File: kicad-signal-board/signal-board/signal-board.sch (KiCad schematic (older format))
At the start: 24 parts, among them IC1 74HCT245, U1 ESP32-DEVKITC-32D

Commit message: BOM made
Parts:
- removed I2C, TX/RX, sig1, sig2, sig3, sig4, sig5, sig6, sig7, sig8: signal, symbol Connector:Conn_01x02_Male
- added C3, C4: 0.1µF, symbol Device:CP1_Small
- added J1: Conn_02x09_Odd_Even, symbol Connector_Generic:Conn_02x09_Odd_Even
- added J?: Conn_02x08_Odd_Even, symbol Connector_Generic:Conn_02x08_Odd_Even
- added R10, R12: 1k, symbol Device:R_Small_US
- added R11, R13: 10k, symbol Device:R_Small_US
- added SW1, SW2: SW_MEC_5G, symbol Switch:SW_MEC_5G
- gave numbers to parts that had none: 3
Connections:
- wire segments 89 -> 135
- no-connect marks 5 -> 9
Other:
- note removed: "cap and resistor for led\n cap - .1 microferads, 100 nanoferads, 0804 / 1206\n resistor - 150 ohm\nconnect some io pins to jumpers\ntwo buttons - hardware debounce\n\n\n\n"

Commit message: some footprints
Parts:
- R1: renamed from R10; footprint (none) -> Resistor_SMD:R_0805_2012Metric_Pad1.15x1.40mm_HandSolder
- R10: renamed from R5; footprint (none) -> Resistor_SMD:R_0805_2012Metric_Pad1.15x1.40mm_HandSolder
- R11: renamed from R6; footprint (none) -> Resistor_SMD:R_0805_2012Metric_Pad1.15x1.40mm_HandSolder
- R12: renamed from R7; footprint (none) -> Resistor_SMD:R_0805_2012Metric_Pad1.15x1.40mm_HandSolder
- R13: renamed from R8; footprint (none) -> Resistor_SMD:R_0805_2012Metric_Pad1.15x1.40mm_HandSolder
- R2: renamed from R11; footprint (none) -> Resistor_SMD:R_0805_2012Metric_Pad1.15x1.40mm_HandSolder
- R3: renamed from R12; footprint (none) -> Resistor_SMD:R_0805_2012Metric_Pad1.15x1.40mm_HandSolder
- R4: renamed from R9; footprint (none) -> Resistor_SMD:R_0805_2012Metric_Pad1.15x1.40mm_HandSolder
- R5: renamed from R13; footprint (none) -> Resistor_SMD:R_0805_2012Metric_Pad1.15x1.40mm_HandSolder
- R6: renamed from R1; footprint (none) -> Resistor_SMD:R_0805_2012Metric_Pad1.15x1.40mm_HandSolder
- R7: renamed from R2; footprint (none) -> Resistor_SMD:R_0805_2012Metric_Pad1.15x1.40mm_HandSolder
- R8: renamed from R3; footprint (none) -> Resistor_SMD:R_0805_2012Metric_Pad1.15x1.40mm_HandSolder
- R9: renamed from R4; footprint (none) -> Resistor_SMD:R_0805_2012Metric_Pad1.15x1.40mm_HandSolder
- gave numbers to parts that had none: 1
- renumbered C3 to C1, C4 to C2, C2 to C3, C1 to C4, SW2 to SW1, SW1 to SW2
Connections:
- net labels added: +5V
- net labels removed: 5v, GNDREF
- wire segments 135 -> 138
- no-connect marks 9 -> 13
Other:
- moved on the sheet: C1, C2, C3, C4, D1, J1, J2, R1, R10, R11, R12, R13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

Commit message: Copied power supply circuit into signal board schematic, initial creation of PCB
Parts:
- added C5: 100uF, Capacitor_THT:CP_Radial_D5.0mm_P2.50mm, symbol Device:CP1_Small
- added C6: 470pF, Capacitor_SMD:C_1206_3216Metric_Pad1.42x1.75mm_HandSolder, symbol Device:CP1_Small
- added C7: 220uF, Capacitor_SMD:CP_Elec_10x10, symbol Device:CP1_Small
- added D2: 1N5819, Diode_SMD:D_SOD-123, symbol Device:D_Schottky
- added J3: 5V Pwr Conn, Connector_PinHeader_1.00mm:PinHeader_1x02_P1.00mm_Vertical, symbol Connector:Conn_01x02_Male
- added J4: 24V Screw Term, TerminalBlock_TE-Connectivity:TerminalBlock_TE_282834-2_1x02_P2.54mm_Horizontal, symbol Connector:Screw_Terminal_01x02
- added L1: 220uH, Inductor_SMD:L_Bourns-SRR1005, symbol Device:L
- added R14: 0.33 ohms, Resistor_SMD:R_0805_2012Metric_Pad1.15x1.40mm_HandSolder, symbol Device:R_Small_US
- added R15: 1.2K, Resistor_SMD:R_0805_2012Metric_Pad1.15x1.40mm_HandSolder, symbol Device:R_Small_US
- added R16: 3.8K, Resistor_SMD:R_0805_2012Metric_Pad1.15x1.40mm_HandSolder, symbol Device:R_Small_US
- added U2: MC33063AD, Package_SO:SOIC-8_3.9x4.9mm_P1.27mm, symbol Regulator_Switching:MC33063AD
- IC1: symbol 74HCT245:74HCT245 -> signal-board-rescue:74HCT245-74HCT245
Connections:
- net labels added: +24V, 5V_Out, 7V_to_24V_Input, Switching_Power_Supply
- wire segments 138 -> 178
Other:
- moved on the sheet: C1, C2, C3, C4, D1, J1, J2, R1, R10, R11, R12, R13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

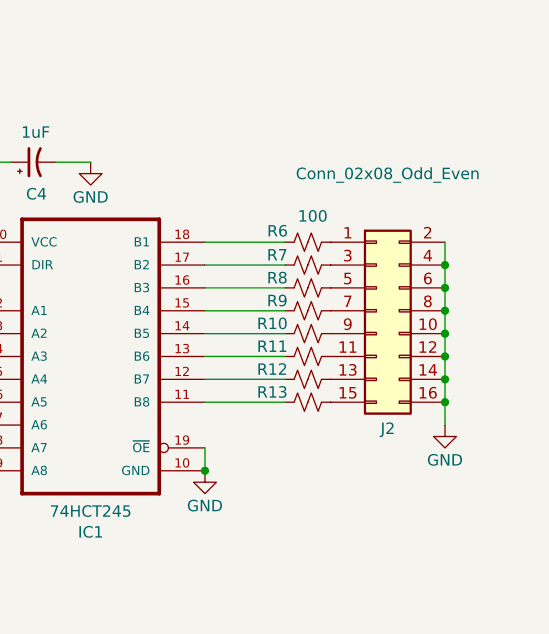
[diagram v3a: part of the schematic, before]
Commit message: More footprints and rough layout of pcb
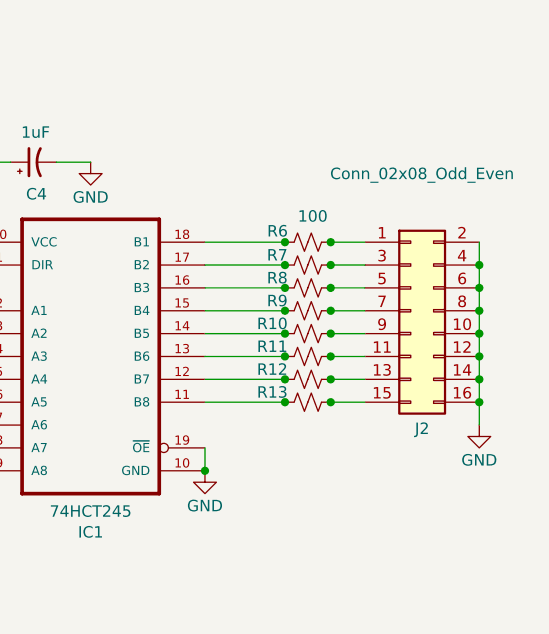
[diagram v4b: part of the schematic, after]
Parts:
- C1, C3: footprint (none) -> Capacitor_SMD:C_0805_2012Metric_Pad1.15x1.40mm_HandSolder
- C2: footprint (none) -> Capacitor_SMD:C_0805_2012Metric_Pad1.15x1.40mm_HandSolder; Supplier Part 08055C104KAT2A -> 478-1395-1-ND
- C4: footprint (none) -> Capacitor_SMD:C_0805_2012Metric_Pad1.15x1.40mm_HandSolder; Supplier Part CC0805KKX7R7BB105 -> 311-1365-1-ND
- IC1: footprint (none) -> Package_SO:SOIC-20W_7.5x12.8mm_P1.27mm
- J1: footprint (none) -> Connector_PinHeader_2.54mm:PinHeader_2x09_P2.54mm_Vertical
- J2: footprint (none) -> Connector_PinHeader_2.54mm:PinHeader_2x08_P2.54mm_Vertical
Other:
- moved on the sheet: J2
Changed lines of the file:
@@
 Connection ~ 4050 3700
 Connection ~ 4050 3800
-Connection ~ 10750 3050
-Connection ~ 10750 3150
-Connection ~ 10750 3250
-Connection ~ 10750 3350
-Connection ~ 10750 3450
-Connection ~ 10750 3550
-Connection ~ 10750 3650
+Connection ~ 10900 3050
+Connection ~ 10900 3150
+Connection ~ 10900 3250
+Connection ~ 10900 3350
+Connection ~ 10900 3450
+Connection ~ 10900 3550
+Connection ~ 10900 3650
 Connection ~ 4050 3300
 Connection ~ 9700 3950
@@
 	9700 3850 9700 3950
 Wire Wire Line
-	10750 2950 10750 3050
-Wire Wire Line
-	10750 3050 10750 3150
-Wire Wire Line
-	10750 3150 10750 3250
-Wire Wire Line
-	10750 3250 10750 3350
-Wire Wire Line
-	10750 3350 10750 3450
-Wire Wire Line
-	10750 3450 10750 3550
-Wire Wire Line
-	10750 3550 10750 3650
-Wire Wire Line
-	10750 3650 10750 3750
+	10900 2950 10900 3050
+Wire Wire Line
+	10900 3050 10900 3150
+Wire Wire Line
+	10900 3150 10900 3250
+Wire Wire Line
+	10900 3250 10900 3350
+Wire Wire Line
+	10900 3350 10900 3450
+Wire Wire Line
+	10900 3450 10900 3550
+Wire Wire Line
+	10900 3550 10900 3650
+Wire Wire Line
+	10900 3650 10900 3750
 Text Notes -3450 5300 0    50   ~ 0
 FASTLED valid pins\nhttps://github.com/FastLED/FastLED/blob/master/platforms/esp/32/fastpin_esp32.h\n\n0\n- 1 - (WARNING - using TX causes flashness when uploading)\n2\n- 3 - (WARNING - using RX causes flashness when uploading)\n4\n5 (leds)\n- 6 - NOPE\n- 7 - NOPE\n- 8 - NOPE\n- 9 - NOPE\n- 10 - NOPE\n- 11 - NOPE\n12 (leds)\n13 (leds)\n14 \n15 (leds)\n16\n17 (leds)\n18 (leds)\n19 (leds)\n- 20 - NOPE\n- 21 - works, but note that 21 is I2C SDA\n- 22 - works, but note that 22 is I2C SCL\n23 (leds)\n- 24 - NOPE\n25 \n26 \n27 \n- 28 - NOPE\n- 29 - NOPE\n- 30 - NOPE\n- 31 - NOPE\n- 32 - note - needs special handling\n- 33 - note - needs special handling\n\n\n\n
@@
 L power:GND #PWR0118
 U 1 1 5E942252
-P 10750 3750
-F 0 "#PWR0118" H 10750 3500 50  0001 C CNN
-F 1 "GND" H 10750 3596 50  0000 C CNN
-F 2 "" H 10750 3750 50  0001 C CNN
-F 3 "" H 10750 3750 50  0001 C CNN
-	1    10750 3750
+P 10900 3750
+F 0 "#PWR0118" H 10900 3500 50  0001 C CNN
+F 1 "GND" H 10900 3596 50  0000 C CNN
+F 2 "" H 10900 3750 50  0001 C CNN
+F 3 "" H 10900 3750 50  0001 C CNN
+	1    10900 3750
 	1    0    0    -1
 $EndComp
@@
 F 0 "C1" H 5110 2837 50  0000 C CNN
 F 1 "0.1µF" H 5450 2832 50  0000 C CNN
-F 2 "" H 5250 2850 50  0001 C CNN
+F 2 "Capacitor_SMD:C_0805_2012Metric_Pad1.15x1.40mm_HandSolder" H 5250 2850 50  0001 C CNN
 F 3 "~" H 5250 2850 50  0001 C CNN
 F 4 "Digikey" H 5250 2850 50  0001 C CNN "Supplier"
@@
 F 0 "C2" H 5560 2137 50  0000 C CNN
 F 1 "0.1µF" H 5900 2132 50  0000 C CNN
-F 2 "" H 5700 2150 50  0001 C CNN
+F 2 "Capacitor_SMD:C_0805_2012Metric_Pad1.15x1.40mm_HandSolder" H 5700 2150 50  0001 C CNN
 F 3 "~" H 5700 2150 50  0001 C CNN
 F 4 "Digikey" H 5700 2150 50  0001 C CNN "Supplier"
-F 5 "08055C104KAT2A" H 5700 2150 50  0001 C CNN "Supplier Part"
+F 5 "478-1395-1-ND" H 5700 2150 50  0001 C CNN "Supplier Part"
 	1    5700 2150
 	1    0    0    -1
@@
 F 0 "C3" V 5860 5387 50  0000 C CNN
 F 1 "0.1µF" V 6130 5391 50  0000 C CNN
-F 2 "" H 6000 5400 50  0001 C CNN
+F 2 "Capacitor_SMD:C_0805_2012Metric_Pad1.15x1.40mm_HandSolder" H 6000 5400 50  0001 C CNN
 F 3 "~" H 6000 5400 50  0001 C CNN
 F 4 "Digikey" H 6000 5400 50  0001 C CNN "Supplier"
@@
 F 0 "C4" V 8810 2587 50  0000 C CNN
 F 1 "1uF" V 9080 2591 50  0000 C CNN
-F 2 "" H 8950 2600 50  0001 C CNN
+F 2 "Capacitor_SMD:C_0805_2012Metric_Pad1.15x1.40mm_HandSolder" H 8950 2600 50  0001 C CNN
 F 3 "~" H 8950 2600 50  0001 C CNN
 F 4 "digikey" H 8950 2600 50  0001 C CNN "Supplier"
-F 5 "CC0805KKX7R7BB105" H 8950 2600 50  0001 C CNN "Supplier Part"
+F 5 "311-1365-1-ND" H 8950 2600 50  0001 C CNN "Supplier Part"
 	1    8950 2600
 	0    -1   -1   0
@@
 L Connector_Generic:Conn_02x08_Odd_Even J2
 U 1 1 5E91A548
-P 10450 3250
-F 0 "J2" H 10500 2734 50  0000 C CNN
-F 1 "Conn_02x08_Odd_Even" H 10500 3849 50  0000 C CNN
-F 2 "" H 10450 3250 50  0001 C CNN
-F 3 "~" H 10450 3250 50  0001 C CNN
-	1    10450 3250
+P 10600 3250
+F 0 "J2" H 10650 2734 50  0000 C CNN
+F 1 "Conn_02x08_Odd_Even" H 10650 3849 50  0000 C CNN
+F 2 "Connector_PinHeader_2.54mm:PinHeader_2x08_P2.54mm_Vertical" H 10600 3250 50  0001 C CNN
+F 3 "~" H 10600 3250 50  0001 C CNN
+	1    10600 3250
 	1    0    0    -1
 $EndComp
@@
 F 0 "J1" H 4300 3084 50  0000 C CNN
 F 1 "Conn_02x09_Odd_Even" H 4300 3175 50  0000 C CNN
-F 2 "" H 4250 3700 50  0001 C CNN
+F 2 "Connector_PinHeader_2.54mm:PinHeader_2x09_P2.54mm_Vertical" H 4250 3700 50  0001 C CNN
 F 3 "~" H 4250 3700 50  0001 C CNN
 	1    4250 3700
@@
 F 0 "IC1" H 9200 2681 50  0000 C CNN
 F 1 "74HCT245" H 9200 2772 50  0000 C CNN
-F 2 "" H 9200 3450 50  0001 C CNN
+F 2 "Package_SO:SOIC-20W_7.5x12.8mm_P1.27mm" H 9200 3450 50  0001 C CNN
 F 3 "" H 9200 3450 50  0001 C CNN
 F 4 "Digikey" H 9200 3450 50  0001 C CNN "Supplier"
@@
 Wire Wire Line
 	1350 7300 1350 7350
+Wire Wire Line
+	10250 2950 10400 2950
+Wire Wire Line
+	10250 3050 10400 3050
+Wire Wire Line
+	10250 3150 10400 3150
+Wire Wire Line
+	10250 3250 10400 3250
+Wire Wire Line
+	10250 3350 10400 3350
+Wire Wire Line
+	10250 3450 10400 3450
+Wire Wire Line
+	10250 3550 10400 3550
+Wire Wire Line
+	10250 3650 10400 3650
+Connection ~ 10050 3350
+Connection ~ 10050 3450
+Connection ~ 10050 3550
+Connection ~ 10050 3650
+Connection ~ 10250 3650
+Connection ~ 10250 3550
+Connection ~ 10250 3450
+Connection ~ 10250 3350
+Connection ~ 10250 3250
+Connection ~ 10250 3150
+Connection ~ 10250 3050
+Connection ~ 10250 2950
+Connection ~ 10050 2950
+Connection ~ 10050 3050
+Connection ~ 10050 3150
+Connection ~ 10050 3250
 $EndSCHEMATC

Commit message: traces 1.0 done
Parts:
- IC1: symbol signal-board-rescue:74HCT245-74HCT245 -> signal-board-rescue:74HCT245-74HCT245-signal-board-rescue
- SW1, SW2: footprint (none) -> PTS525SM15SMTR2LFS:SW_PTS525SM15SMTR2LFS
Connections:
- net GND: now also J1.15 (Pin_15), J1.17 (Pin_17); no longer J1.1 (Pin_1), J1.3 (Pin_3)
- net at D1.1 (DOUT): now also J2.1 (Pin_1)
- net at D1.2 (DIN): now also R6.2; no longer U1.12 (IO14)
- net at C2.1, R3.2, R5.2: now also U1.6 (IO35); no longer U1.5 (IO34)
- net at U1.10 (IO26): now also J1.16 (Pin_16); no longer J1.12 (Pin_12)
- net at U1.11 (IO27): now also J1.18 (Pin_18); no longer J1.14 (Pin_14)
- net at U1.22 (IO22): now also J1.1 (Pin_1); no longer J1.15 (Pin_15)
- net at U1.23 (TXD0): now also J1.3 (Pin_3); no longer J1.17 (Pin_17)
- net at U1.24 (RXD0): now also J1.4 (Pin_4); no longer J1.18 (Pin_18)
- net at U1.25 (IO21): now also J1.2 (Pin_2); no longer J1.16 (Pin_16)
- net at U1.3 (SENSOR_VP): now also J1.6 (Pin_6); no longer J1.2 (Pin_2)
- net at U1.4 (SENSOR_VN): now also J1.8 (Pin_8); no longer J1.4 (Pin_4)
- net at C1.1, R1.2, R2.2: now also U1.5 (IO34); no longer U1.6 (IO35)
- net at U1.7 (IO32): now also J1.10 (Pin_10); no longer J1.6 (Pin_6)
- net at U1.8 (IO33): now also J1.12 (Pin_12); no longer J1.8 (Pin_8)
- net at U1.9 (IO25): now also J1.14 (Pin_14); no longer J1.10 (Pin_10)
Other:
- moved on the sheet: C3, D1, R4

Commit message: Updated packages footprints and added ground plane stitching
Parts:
- C5: footprint Capacitor_THT:CP_Radial_D5.0mm_P2.50mm -> Capacitor_SMD:C_Elec_6.3x7.7
- IC1: footprint Package_SO:SOIC-20W_7.5x12.8mm_P1.27mm -> 74HCD245:SOIC-20W_7.5x10.0mm_P1.27mm
- L1: footprint Inductor_SMD:L_Bourns-SRR1005 -> Inductor_SMD:L_Bourns_SDR1806
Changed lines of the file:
@@
+$EndComp
+$Comp
+L Device:L L?
+U 1 1 5E87C810
+P 4300 8550
+AR Path="/5E86A5CD/5E87C810" Ref="L?"  Part="1"
+AR Path="/5E87C810" Ref="L1"  Part="1"
+F 0 "L1" H 4352 8596 50  0000 L CNN
+F 1 "220uH" H 4352 8505 50  0000 L CNN
+F 2 "Inductor_SMD:L_Bourns_SDR1806" H 4300 8550 50  0001 C CNN
+F 3 "~" H 4300 8550 50  0001 C CNN
+F 4 "Digikey" H 4300 8550 50  0001 C CNN "Supplier"
+F 5 "SDR1806-221KLCT-ND" H 4300 8550 50  0001 C CNN "Supplier Part"
+	1    4300 8550
+	1    0    0    -1
 $EndComp
 $Comp
@@
 F 3 "" H 11150 1600 50  0001 C CNN
 	1    11150 1600
-	1    0    0    -1
-$EndComp
-$Comp
-L Device:L L?
-U 1 1 5E87C810
-P 4300 8550
-AR Path="/5E86A5CD/5E87C810" Ref="L?"  Part="1"
-AR Path="/5E87C810" Ref="L1"  Part="1"
-F 0 "L1" H 4352 8596 50  0000 L CNN
-F 1 "220uH" H 4352 8505 50  0000 L CNN
-F 2 "Inductor_SMD:L_Bourns-SRR1005" H 4300 8550 50  0001 C CNN
-F 3 "~" H 4300 8550 50  0001 C CNN
-F 4 "Digikey" H 4300 8550 50  0001 C CNN "Supplier"
-F 5 "SDR1806-221KLCT-ND" H 4300 8550 50  0001 C CNN "Supplier Part"
-	1    4300 8550
 	1    0    0    -1
 $EndComp
@@
 F 0 "C5" H 1891 8246 50  0000 L CNN
 F 1 "100uF" H 1891 8155 50  0000 L CNN
-F 2 "Capacitor_THT:CP_Radial_D5.0mm_P2.50mm" H 1800 8200 50  0001 C CNN
+F 2 "Capacitor_SMD:C_Elec_6.3x7.7" H 1800 8200 50  0001 C CNN
 F 3 "~" H 1800 8200 50  0001 C CNN
 F 4 "493-2203-1-ND" H 1800 8200 50  0001 C CNN "Supplier Part"
@@
 $EndComp
 $Comp
+L Connector_Generic:Conn_02x09_Odd_Even J1
+U 1 1 5E90F867
+P 4250 3700
+F 0 "J1" H 4300 3084 50  0000 C CNN
+F 1 "Conn_02x09_Odd_Even" H 4300 3175 50  0000 C CNN
+F 2 "Connector_PinHeader_2.54mm:PinHeader_2x09_P2.54mm_Vertical" H 4250 3700 50  0001 C CNN
+F 3 "~" H 4250 3700 50  0001 C CNN
+	1    4250 3700
+	1    0    0    -1
+$EndComp
+$Comp
 L Regulator_Switching:MC33063AD U?
 U 1 1 5E87C86F
@@
 $EndComp
 $Comp
-L Connector_Generic:Conn_02x09_Odd_Even J1
-U 1 1 5E90F867
-P 4250 3700
-F 0 "J1" H 4300 3084 50  0000 C CNN
-F 1 "Conn_02x09_Odd_Even" H 4300 3175 50  0000 C CNN
-F 2 "Connector_PinHeader_2.54mm:PinHeader_2x09_P2.54mm_Vertical" H 4250 3700 50  0001 C CNN
-F 3 "~" H 4250 3700 50  0001 C CNN
-	1    4250 3700
-	1    0    0    -1
-$EndComp
-$Comp
 L signal-board-rescue:74HCT245-74HCT245-signal-board-rescue IC1
 U 1 1 5E984FA4
@@
 F 0 "IC1" H 9200 2681 50  0000 C CNN
 F 1 "74HCT245" H 9200 2772 50  0000 C CNN
-F 2 "Package_SO:SOIC-20W_7.5x12.8mm_P1.27mm" H 9200 3450 50  0001 C CNN
+F 2 "74HCD245:SOIC-20W_7.5x10.0mm_P1.27mm" H 9200 3450 50  0001 C CNN
 F 3 "" H 9200 3450 50  0001 C CNN
 F 4 "Digikey" H 9200 3450 50  0001 C CNN "Supplier"

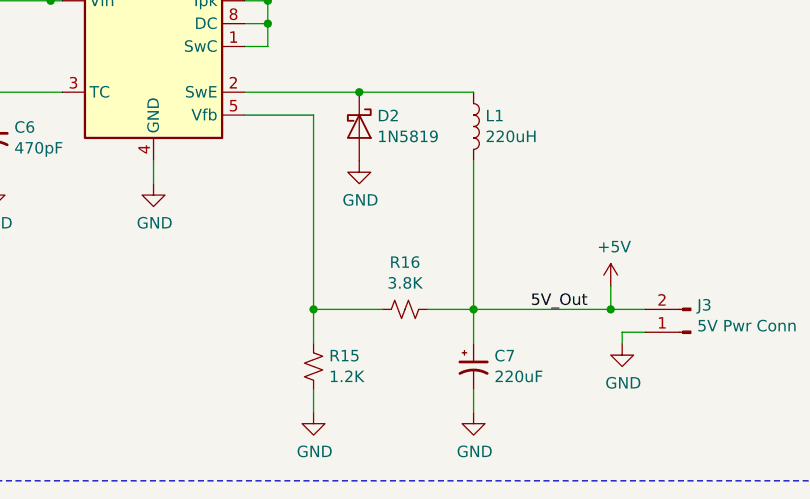
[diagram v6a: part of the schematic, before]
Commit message: Updated resistor part numbers on feedback circuit for power supply
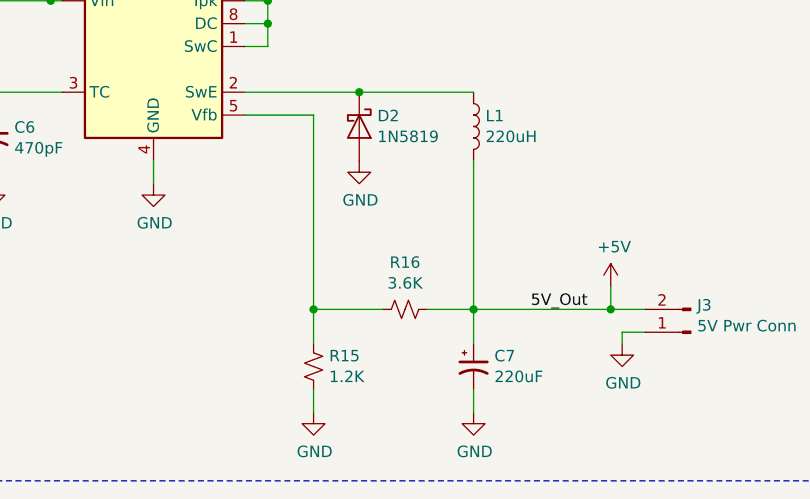
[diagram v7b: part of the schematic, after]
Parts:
- R15: Supplier Part 311-1.20KCRCT-ND -> P123801CT-ND
- R16: value 3.8K -> 3.6K; Supplier Part P3.83KCCT-ND -> P123841CT-ND
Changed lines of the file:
@@
 F 2 "Resistor_SMD:R_0805_2012Metric_Pad1.15x1.40mm_HandSolder" H 3600 9600 50  0001 C CNN
 F 3 "~" H 3600 9600 50  0001 C CNN
-F 4 "311-1.20KCRCT-ND" H 3600 9600 50  0001 C CNN "Supplier Part"
+F 4 "P123801CT-ND" H 3600 9600 50  0001 C CNN "Supplier Part"
 F 5 "DigiKey" H 3600 9600 50  0001 C CNN "Supplier"
 	1    3600 9600
@@
 AR Path="/5E87C7FE" Ref="R16"  Part="1"
 F 0 "R16" V 4205 9350 50  0000 C CNN
-F 1 "3.8K" V 4114 9350 50  0000 C CNN
+F 1 "3.6K" V 4114 9350 50  0000 C CNN
 F 2 "Resistor_SMD:R_0805_2012Metric_Pad1.15x1.40mm_HandSolder" H 4000 9350 50  0001 C CNN
 F 3 "~" H 4000 9350 50  0001 C CNN
 F 4 "Digikey" V 4000 9350 50  0001 C CNN "Supplier"
-F 5 "P3.83KCCT-ND" V 4000 9350 50  0001 C CNN "Supplier Part"
+F 5 "P123841CT-ND" V 4000 9350 50  0001 C CNN "Supplier Part"
 	1    4000 9350
 	0    -1   -1   0

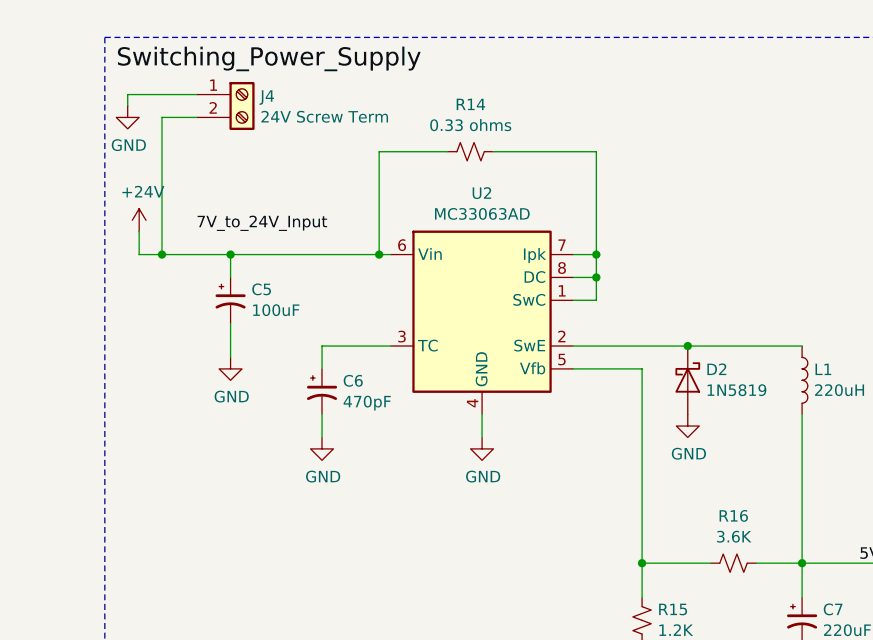
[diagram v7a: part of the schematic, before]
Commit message: Fixed DRC check error with alternate 5V supply footprint using 2.54mm instead of 1.0mm 1x2 header
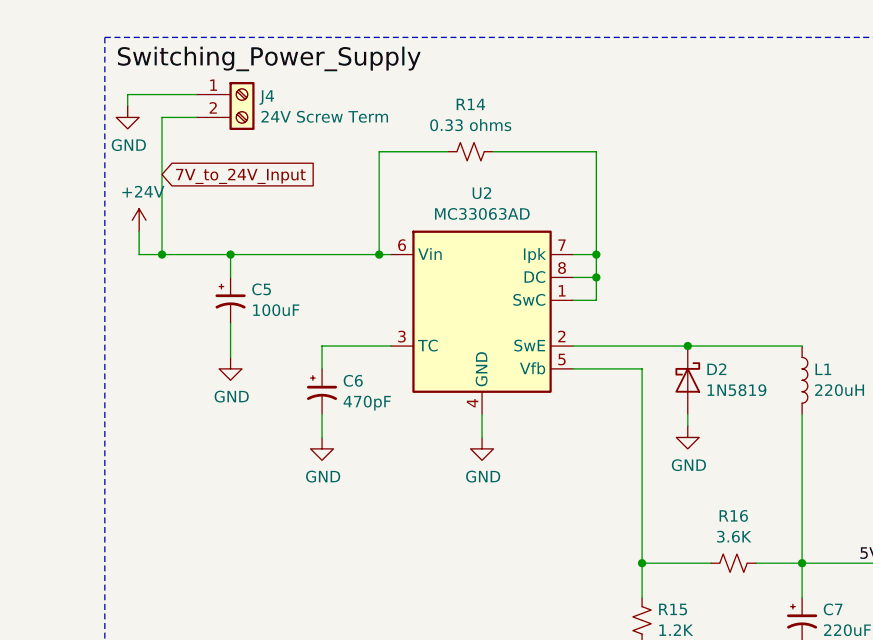
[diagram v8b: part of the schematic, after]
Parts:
- J3: footprint Connector_PinHeader_1.00mm:PinHeader_1x02_P1.00mm_Vertical -> Connector_PinHeader_2.54mm:PinHeader_1x02_P2.54mm_Vertical
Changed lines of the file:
@@
 	3800 8400 4300 8400
+Wire Wire Line
+	3800 8700 3800 8750
 Wire Wire Line
 	3850 3500 4050 3500
@@
 Text Label 1300 7200 0    79   ~ 0
 Switching_Power_Supply
-Text Label 1650 7900 0    50   ~ 0
-7V_to_24V_Input
 Text Label 4550 9350 0    50   ~ 0
 5V_Out
+Text GLabel 1500 7650 2    50   Input ~ 0
+7V_to_24V_Input
 $Comp
 L power:+24V #PWR?
@@
 L power:GND #PWR?
 U 1 1 5E87C832
-P 3800 8700
+P 3800 8750
 AR Path="/5E86A5CD/5E87C832" Ref="#PWR?"  Part="1"
 AR Path="/5E87C832" Ref="#PWR0123"  Part="1"
-F 0 "#PWR0123" H 3800 8450 50  0001 C CNN
-F 1 "GND" H 3805 8527 50  0000 C CNN
-F 2 "" H 3800 8700 50  0001 C CNN
-F 3 "" H 3800 8700 50  0001 C CNN
-	1    3800 8700
+F 0 "#PWR0123" H 3800 8500 50  0001 C CNN
+F 1 "GND" H 3805 8577 50  0000 C CNN
+F 2 "" H 3800 8750 50  0001 C CNN
+F 3 "" H 3800 8750 50  0001 C CNN
+	1    3800 8750
 	1    0    0    -1
 $EndComp
@@
 F 0 "J3" H 5222 9332 50  0000 R CNN
 F 1 "5V Pwr Conn" H 5222 9423 50  0000 R CNN
-F 2 "Connector_PinHeader_1.00mm:PinHeader_1x02_P1.00mm_Vertical" H 5250 9450 50  0001 C CNN
+F 2 "Connector_PinHeader_2.54mm:PinHeader_1x02_P2.54mm_Vertical" H 5250 9450 50  0001 C CNN
 F 3 "~" H 5250 9450 50  0001 C CNN
 	1    5250 9450
